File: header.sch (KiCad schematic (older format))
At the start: 47 parts, among them J1 Conn_01x10, J2 Conn_01x08, J3 Conn_01x06, J4 Conn_01x08, Q2 Q_NMOS_GSD, Q3 Q_NMOS_GSD, Q4 Q_NMOS_GSD, SW6 SW_Push, U1 ICE40HX4K-TQ144, U20 MAX11614, U22 MAX40200AUK, U23 MAX40200AUK, U8 TXS0108EPW, U9 TXS0108EPW, Y2 ECS-3225S33-500-FN-TR

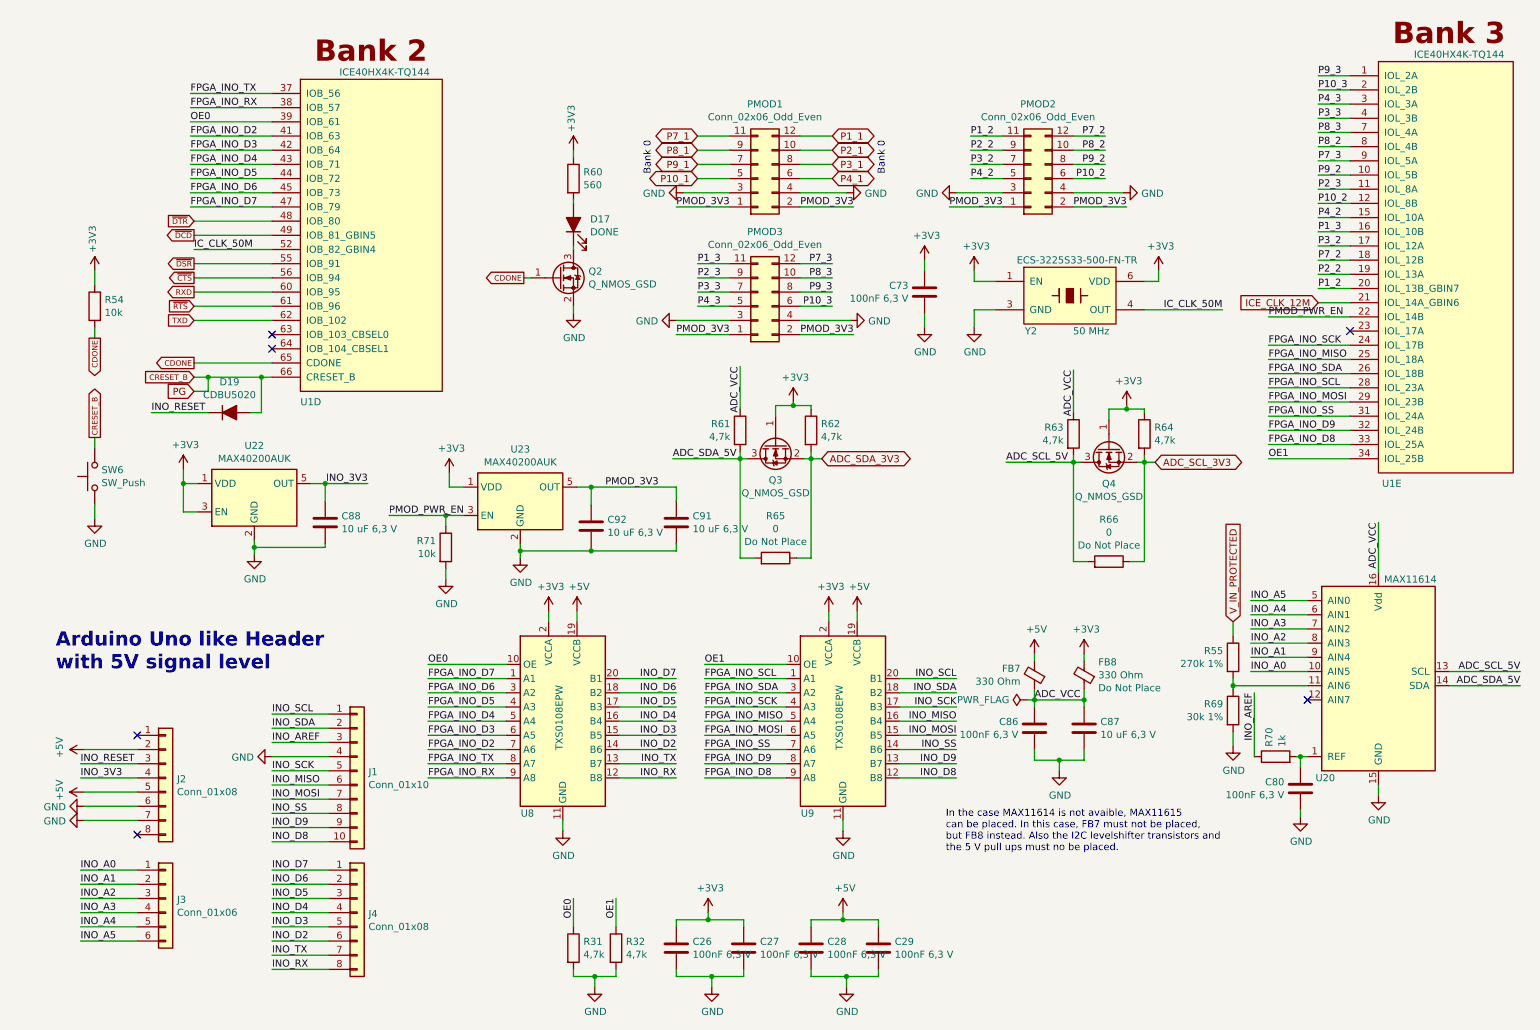
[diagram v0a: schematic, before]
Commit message: Schematic modified (Hierarchy) Bug where SPI was active when creset or ss was low fixed PCB layout started (almost all parts are at position) No parts on the bottom so far Arduino and PMOD header spacings corrected according to its standards
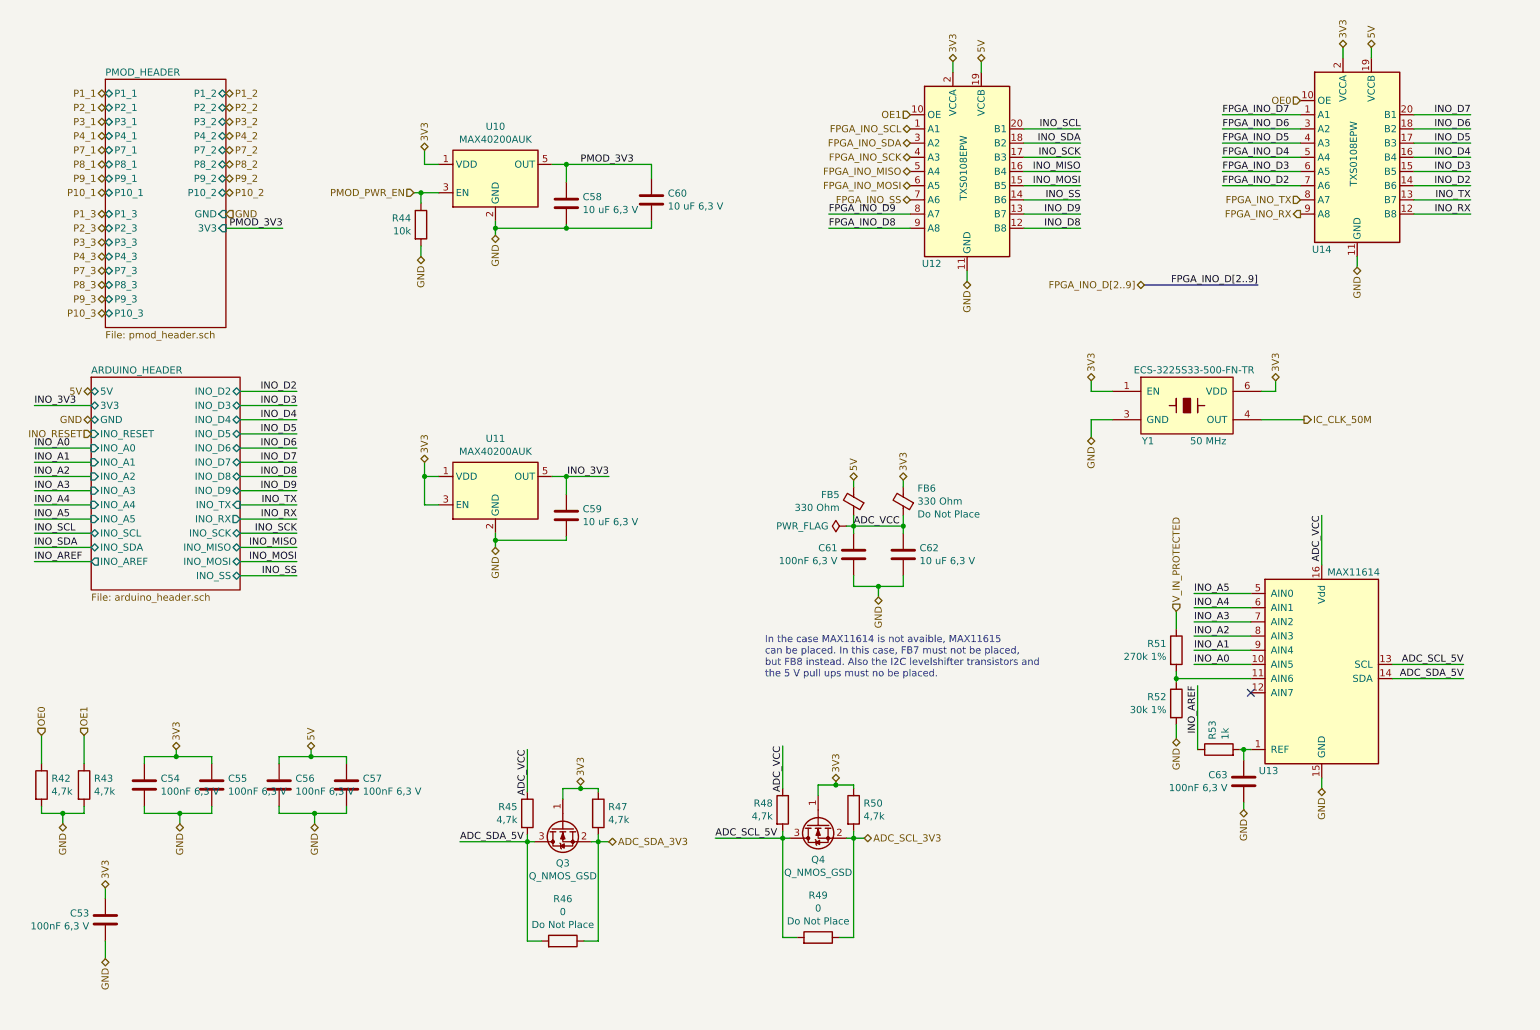
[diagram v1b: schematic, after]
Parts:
- removed D17: DONE, LED_SMD:LED_0603_1608Metric, symbol Device:LED_ALT
- removed D19: CDBU5020, Diode_SMD:D_0603_1608Metric, symbol Device:D_ALT
- removed J1: Conn_01x10, Connector_PinSocket_2.54mm:PinSocket_1x10_P2.54mm_Vertical, symbol Connector_Generic:Conn_01x10
- removed J2, J4: Conn_01x08, Connector_PinSocket_2.54mm:PinSocket_1x08_P2.54mm_Vertical, symbol Connector_Generic:Conn_01x08
- removed J3: Conn_01x06, Connector_PinSocket_2.54mm:PinSocket_1x06_P2.54mm_Vertical, symbol Connector_Generic:Conn_01x06
- removed PMOD1, PMOD2, PMOD3: Conn_02x06_Odd_Even, Connector_PinSocket_2.54mm:PinSocket_2x06_P2.54mm_Horizontal, symbol Connector_Generic:Conn_02x06_Odd_Even
- removed Q2: Q_NMOS_GSD, Package_TO_SOT_SMD:SOT-23, symbol Device:Q_NMOS_GSD
- removed R54: 10k, Resistor_SMD:R_0603_1608Metric, symbol Device:R
- removed R60: 560, Resistor_SMD:R_0603_1608Metric, symbol Device:R
- removed SW6: SW_Push, footprints:SW_SPST_TL3305A, symbol Switch:SW_Push
- removed U1: ICE40HX4K-TQ144, symbol ice40hx4k:ICE40HX4K-TQ144
- renumbered C73 to C53, C26 to C54, C27 to C55, C28 to C56, C29 to C57, C92 to C58, C88 to C59, C91 to C60, C86 to C61, C87 to C62, C80 to C63, FB7 to FB5, FB8 to FB6, R31 to R42, R32 to R43, R71 to R44, R61 to R45, R65 to R46, R62 to R47, R63 to R48, R66 to R49, R64 to R50, R55 to R51, R69 to R52, R70 to R53, U23 to U10, U22 to U11, U9 to U12, U20 to U13, U8 to U14, Y2 to Y1
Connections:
- net +3V3 renamed 3V3
- net +5V renamed 5V
- no-connect marks 6 -> 1
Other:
- note removed: "Arduino Uno like Header\nwith 5V signal level"
- note removed: "Bank 0"
- moved on the sheet: C53, C54, C55, C56, C57, C58, C59, C60, C61, C62, C63, FB5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

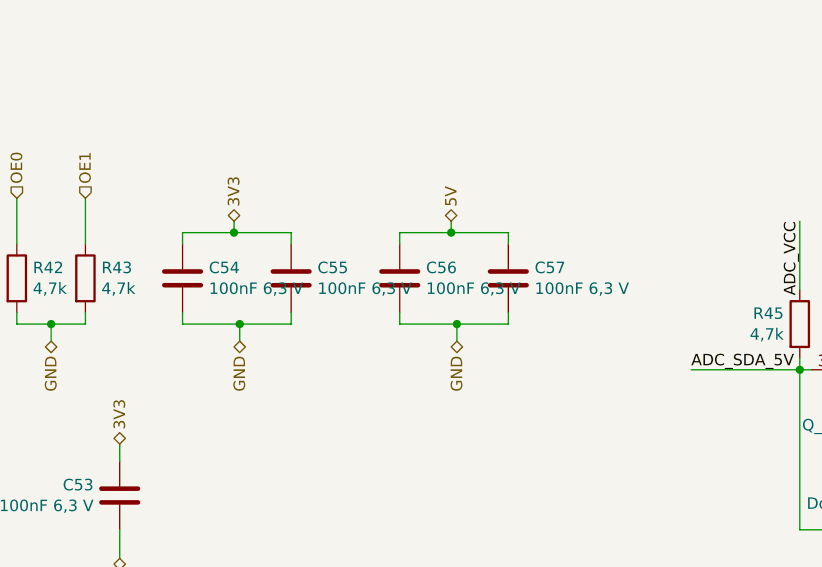
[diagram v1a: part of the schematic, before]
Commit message: 7-17 VIN Power PIN Header moved to the left for better compatibility with extension boards. Added 0 Ohm resistors for optional desoldering of quad-SPI wires. USB power jumper moved more to the side of the board. Arduino Header decoupling capacitors moved to arduino header sheet.
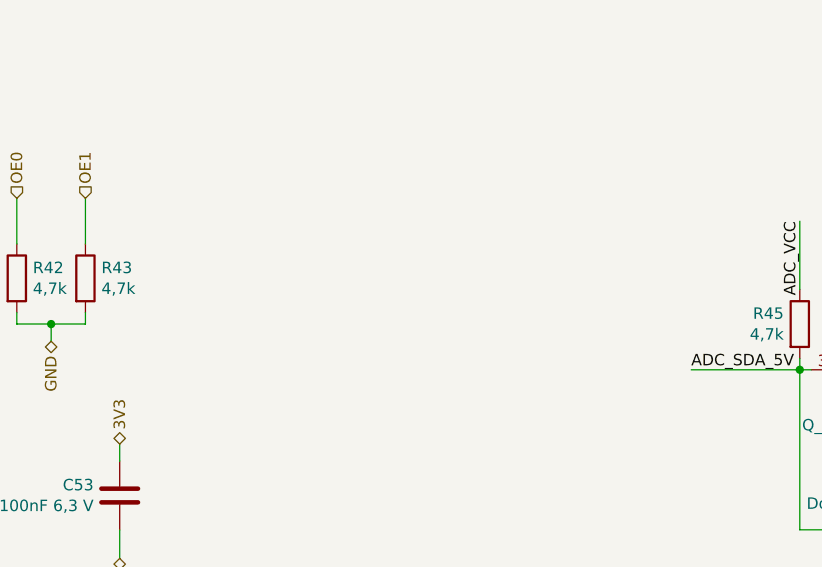
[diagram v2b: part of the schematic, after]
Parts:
- removed C54, C55, C56, C57: 100nF 6,3 V, Capacitor_SMD:C_0603_1608Metric, symbol Device:C
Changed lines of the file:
@@
 	1000 5625 1000 5825
-$Comp
-L Device:C C?
-U 1 1 5CD4ED57
-P 1900 5975
-AR Path="/5CAB7CD4/5CD4ED57" Ref="C?"  Part="1"
-AR Path="/5CB5889B/5CD4ED57" Ref="C?"  Part="1"
-AR Path="/5ED96D61/5CD4ED57" Ref="C55"  Part="1"
-F 0 "C55" H 2015 6021 50  0000 L CNN
-F 1 "100nF 6,3 V" H 2015 5930 50  0000 L CNN
-F 2 "Capacitor_SMD:C_0603_1608Metric" H 1938 5825 50  0001 C CNN
-F 3 "~" H 1900 5975 50  0001 C CNN
-F 4 "CAP CER 0.1UF 50V X7R 0603" H -3750 -1150 50  0001 C CNN "Description"
-F 5 "1276-1000-1-ND" H -3750 -1150 50  0001 C CNN "Digikey"
-F 6 "Samsung Electro-Mechanics" H -3750 -1150 50  0001 C CNN "Mfg Name"
-F 7 "CL10B104KB8NNNC" H -3750 -1150 50  0001 C CNN "Mfg Part Num"
-F 8 "Any" H -3750 -1150 50  0001 C CNN "Spec"
-	1    1900 5975
-	1    0    0    -1
-$EndComp
-Wire Wire Line
-	1425 6125 1425 6175
-Wire Wire Line
-	1425 6175 1675 6175
-Wire Wire Line
-	1900 6175 1900 6125
-Wire Wire Line
-	1675 6250 1675 6175
-Connection ~ 1675 6175
-Wire Wire Line
-	1675 6175 1900 6175
-Wire Wire Line
-	1425 5825 1425 5775
-Wire Wire Line
-	1425 5775 1650 5775
-Wire Wire Line
-	1900 5775 1900 5825
-Wire Wire Line
-	1650 5725 1650 5775
-Connection ~ 1650 5775
-Wire Wire Line
-	1650 5775 1900 5775
-$Comp
-L Device:C C?
-U 1 1 5CD72815
-P 2375 5975
-AR Path="/5CAB7CD4/5CD72815" Ref="C?"  Part="1"
-AR Path="/5CB5889B/5CD72815" Ref="C?"  Part="1"
-AR Path="/5ED96D61/5CD72815" Ref="C56"  Part="1"
-F 0 "C56" H 2490 6021 50  0000 L CNN
-F 1 "100nF 6,3 V" H 2490 5930 50  0000 L CNN
-F 2 "Capacitor_SMD:C_0603_1608Metric" H 2413 5825 50  0001 C CNN
-F 3 "~" H 2375 5975 50  0001 C CNN
-F 4 "CAP CER 0.1UF 50V X7R 0603" H -3750 -1150 50  0001 C CNN "Description"
-F 5 "1276-1000-1-ND" H -3750 -1150 50  0001 C CNN "Digikey"
-F 6 "Samsung Electro-Mechanics" H -3750 -1150 50  0001 C CNN "Mfg Name"
-F 7 "CL10B104KB8NNNC" H -3750 -1150 50  0001 C CNN "Mfg Part Num"
-F 8 "Any" H -3750 -1150 50  0001 C CNN "Spec"
-	1    2375 5975
-	1    0    0    -1
-$EndComp
-$Comp
-L Device:C C?
-U 1 1 5CD7281F
-P 2850 5975
-AR Path="/5CAB7CD4/5CD7281F" Ref="C?"  Part="1"
-AR Path="/5CB5889B/5CD7281F" Ref="C?"  Part="1"
-AR Path="/5ED96D61/5CD7281F" Ref="C57"  Part="1"
-F 0 "C57" H 2965 6021 50  0000 L CNN
-F 1 "100nF 6,3 V" H 2965 5930 50  0000 L CNN
-F 2 "Capacitor_SMD:C_0603_1608Metric" H 2888 5825 50  0001 C CNN
-F 3 "~" H 2850 5975 50  0001 C CNN
-F 4 "CAP CER 0.1UF 50V X7R 0603" H -3750 -1150 50  0001 C CNN "Description"
-F 5 "1276-1000-1-ND" H -3750 -1150 50  0001 C CNN "Digikey"
-F 6 "Samsung Electro-Mechanics" H -3750 -1150 50  0001 C CNN "Mfg Name"
-F 7 "CL10B104KB8NNNC" H -3750 -1150 50  0001 C CNN "Mfg Part Num"
-F 8 "Any" H -3750 -1150 50  0001 C CNN "Spec"
-	1    2850 5975
-	1    0    0    -1
-$EndComp
-Wire Wire Line
-	2375 6125 2375 6175
-Wire Wire Line
-	2375 6175 2625 6175
-Wire Wire Line
-	2850 6175 2850 6125
-Wire Wire Line
-	2625 6250 2625 6175
-Connection ~ 2625 6175
-Wire Wire Line
-	2625 6175 2850 6175
-Wire Wire Line
-	2375 5825 2375 5775
-Wire Wire Line
-	2375 5775 2600 5775
-Wire Wire Line
-	2850 5775 2850 5825
-Wire Wire Line
-	2600 5725 2600 5775
-Connection ~ 2600 5775
-Wire Wire Line
-	2600 5775 2850 5775
-$Comp
-L Device:C C?
-U 1 1 5CD4AF05
-P 1425 5975
-AR Path="/5CAB7CD4/5CD4AF05" Ref="C?"  Part="1"
-AR Path="/5CB5889B/5CD4AF05" Ref="C?"  Part="1"
-AR Path="/5ED96D61/5CD4AF05" Ref="C54"  Part="1"
-F 0 "C54" H 1540 6021 50  0000 L CNN
-F 1 "100nF 6,3 V" H 1540 5930 50  0000 L CNN
-F 2 "Capacitor_SMD:C_0603_1608Metric" H 1463 5825 50  0001 C CNN
-F 3 "~" H 1425 5975 50  0001 C CNN
-F 4 "CAP CER 0.1UF 50V X7R 0603" H -3750 -1150 50  0001 C CNN "Description"
-F 5 "1276-1000-1-ND" H -3750 -1150 50  0001 C CNN "Digikey"
-F 6 "Samsung Electro-Mechanics" H -3750 -1150 50  0001 C CNN "Mfg Name"
-F 7 "CL10B104KB8NNNC" H -3750 -1150 50  0001 C CNN "Mfg Part Num"
-F 8 "Any" H -3750 -1150 50  0001 C CNN "Spec"
-	1    1425 5975
-	1    0    0    -1
-$EndComp
 $Comp
 L ECS-3225S:ECS-3225S33 Y?
@@
 Text HLabel 10075 775  1    50   BiDi ~ 0
 5V
-Text HLabel 1650 5725 1    50   BiDi ~ 0
-3V3
-Text HLabel 2600 5725 1    50   BiDi ~ 0
-5V
 Text HLabel 9975 2325 3    50   BiDi ~ 0
 GND
 Text HLabel 7225 2425 3    50   BiDi ~ 0
 GND
-Text HLabel 2625 6250 3    50   BiDi ~ 0
-GND
-Text HLabel 1675 6250 3    50   BiDi ~ 0
-GND
 Text HLabel 850  6250 3    50   BiDi ~ 0

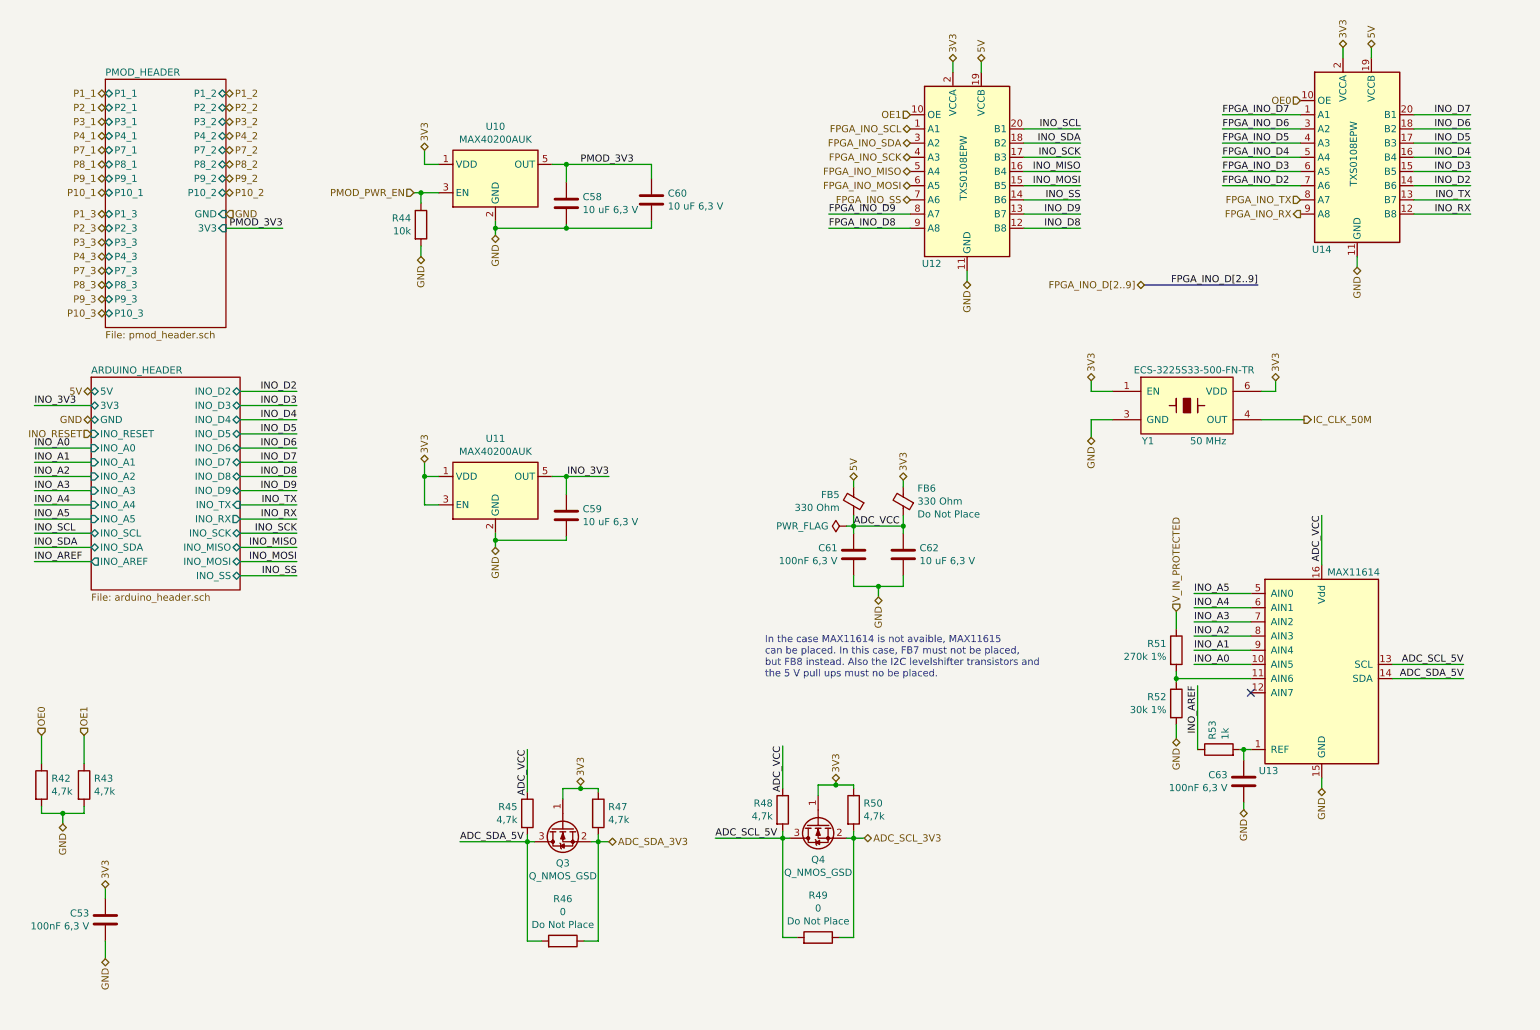
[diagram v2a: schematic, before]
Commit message: Move of decoupling capacitors from last commit reverted (meant for Arduino Header Level Shifters). Component placement complete.
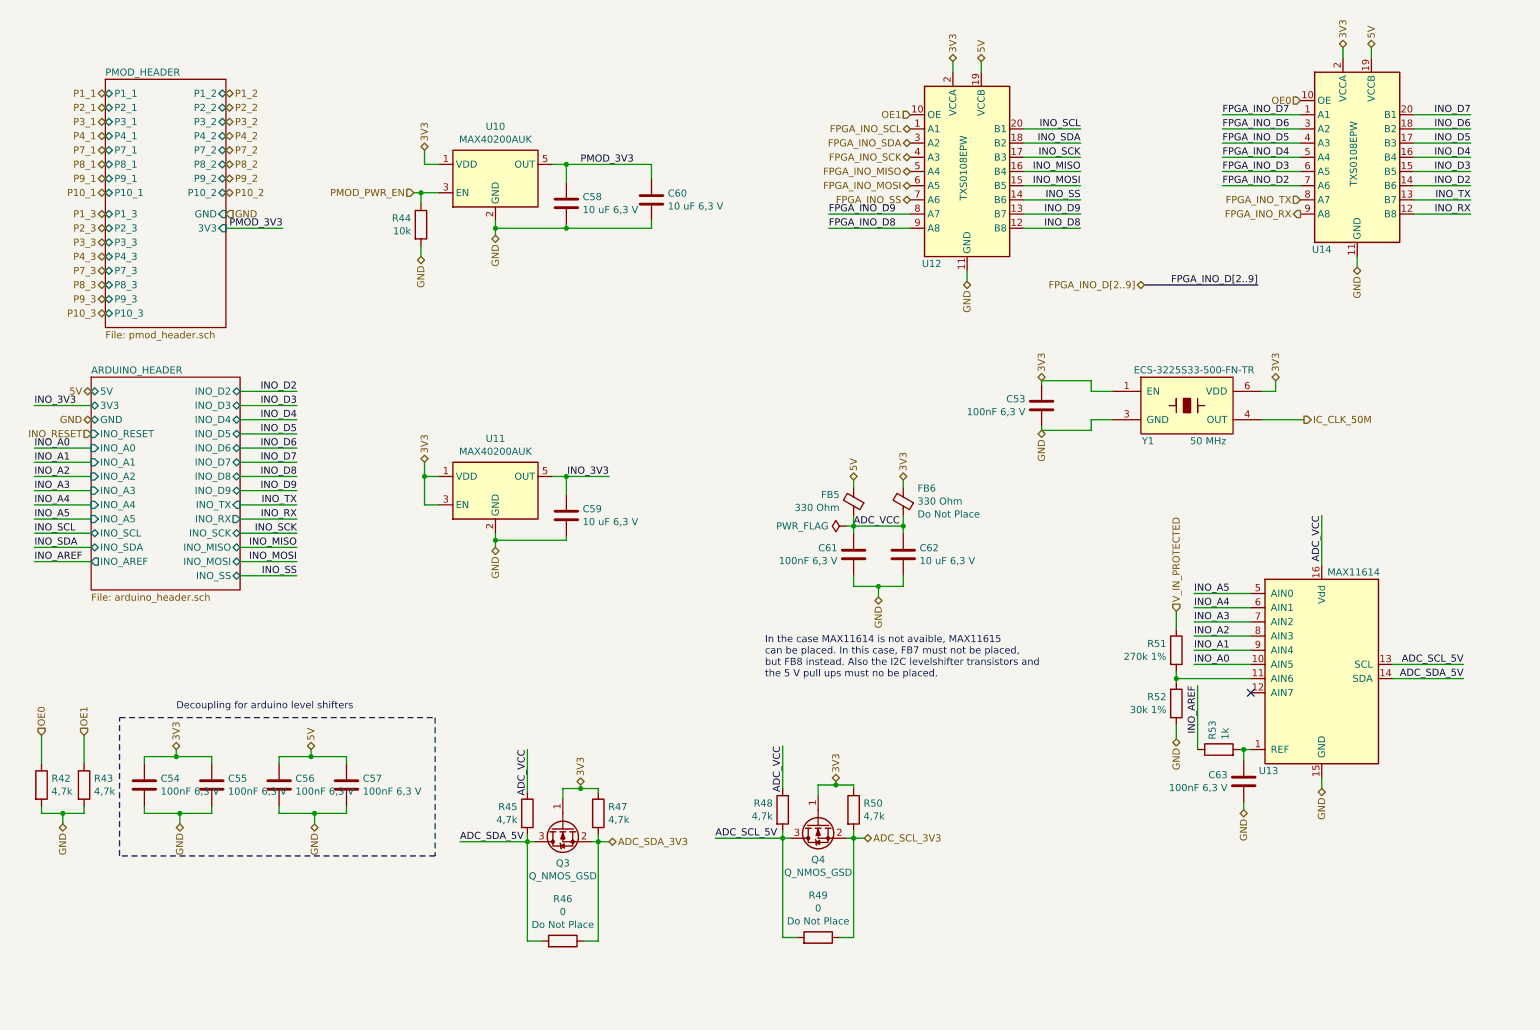
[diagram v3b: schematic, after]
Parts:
- added C54, C55, C56, C57: 100nF 6,3 V, Capacitor_SMD:C_0603_1608Metric, symbol Device:C
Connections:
- net 3V3: now also C54.1, C55.1
- net 5V: now also C56.1, C57.1
- net GND: now also C54.2, C55.2, C56.2, C57.2
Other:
- note added: "Decoupling for arduino level shifters"
- moved on the sheet: C53
